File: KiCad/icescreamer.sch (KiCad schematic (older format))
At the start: 90 parts, among them J1 Audio-Jack-3_3Switches, J2 Audio-Jack-3_3Switches, J3 Barrel_Jack_Switch, Q1 BC547, Q2 BC547, Q20 BC547, Q21 BC547, Q22 BC547, Q23 Q_NJFET_SGD, Q24 Q_NJFET_SGD, SW1 SW_TPDT, SW20 SW_Push, U1 NE5532

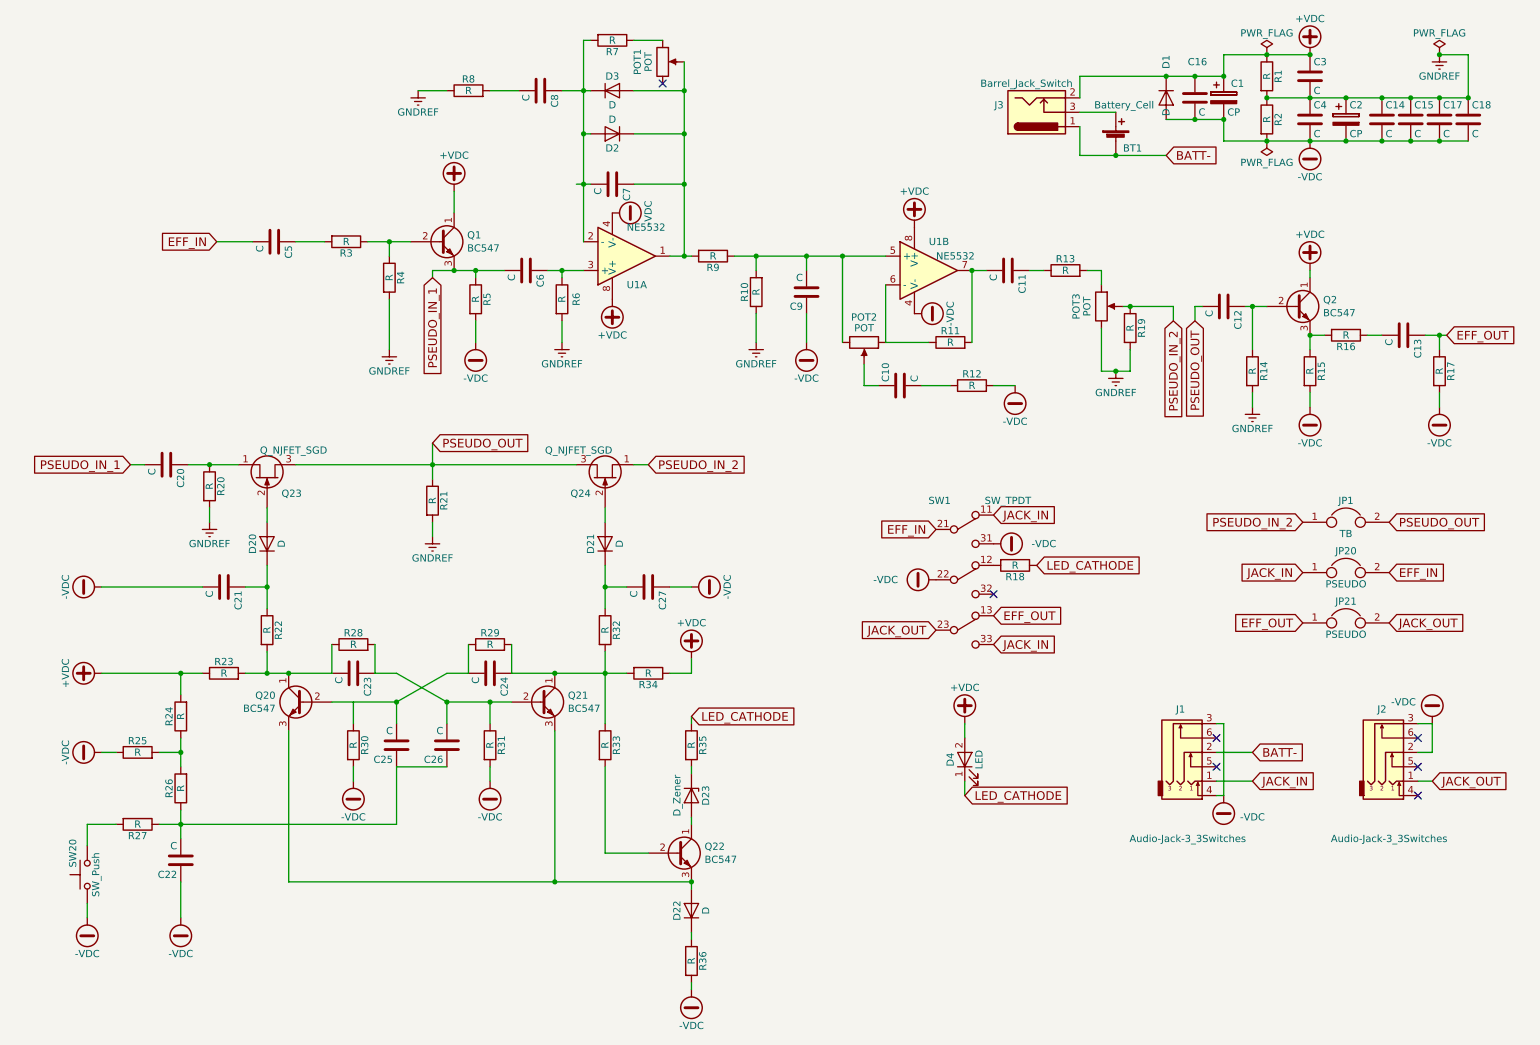
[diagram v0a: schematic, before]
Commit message: añadido BOM interactivo
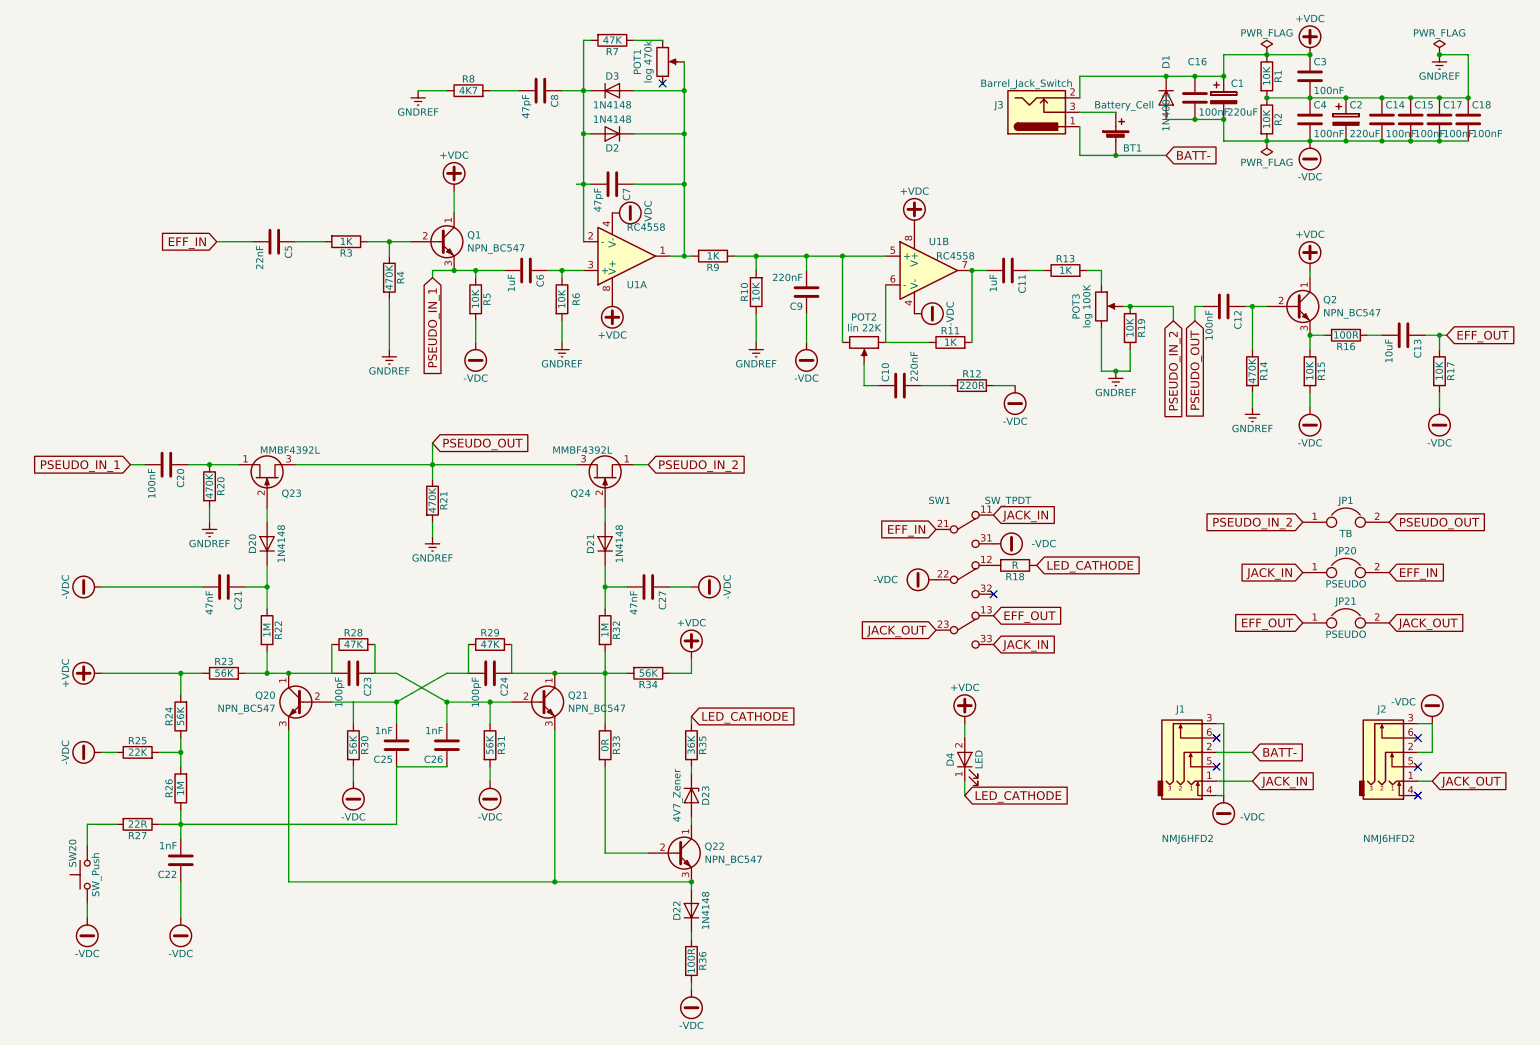
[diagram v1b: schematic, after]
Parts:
- C1, C2: value CP -> 220uF
- C10, C9: value C -> 220nF
- C11, C6: value C -> 1uF
- C12, C14, C15, C16, C17, C18, C20, C3, C4: value C -> 100nF
- C13: value C -> 10uF
- C21, C27: value C -> 47nF
- C22, C25, C26: value C -> 1nF
- C23, C24: value C -> 100pF
- C5: value C -> 22nF
- C7, C8: value C -> 47pF
- D1: value D -> 1N4001
- D2, D20, D21, D22, D3: value D -> 1N4148
- D23: value D_Zener -> 4V7_Zener
- J1, J2: value Audio-Jack-3_3Switches -> NMJ6HFD2
- POT1: value POT -> log 470k
- POT2: value POT -> lin 22K
- POT3: value POT -> log 100K
- Q1, Q2, Q20, Q21, Q22: value BC547 -> NPN_BC547
- Q23, Q24: value Q_NJFET_SGD -> MMBF4392L
- R1, R10, R15, R17, R19, R2, R5, R6: value R -> 10K
- R11, R13, R3, R9: value R -> 1K
- R12: value R -> 220R
- R14, R20, R21, R4: value R -> 470K
- R16, R36: value R -> 100R
- R22, R26, R32: value R -> 1M
- R23, R24, R30, R31, R34: value R -> 56K
- R25: value R -> 22K
- R27: value R -> 22R
- R28, R29, R7: value R -> 47K
- R33: value R -> 0R
- R35: value R -> 36K
- R8: value R -> 4K7
- U1: value NE5532 -> RC4558
